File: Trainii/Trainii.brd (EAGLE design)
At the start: 50.8 x 71.1 mm, 44 parts, among them J1 APDS-9960, J2 Left Motor Encoder, J3 Right Motor Encoder, J4 Line Sensor 1, J5 Line Sensor 2, J6 Ultrasonic, J7 Left Motor Output, J8 Right Motor Output, J9 Lift Motor Output, U1 TPS61222DCKR, U2 BSS138, X1 JST-PH2

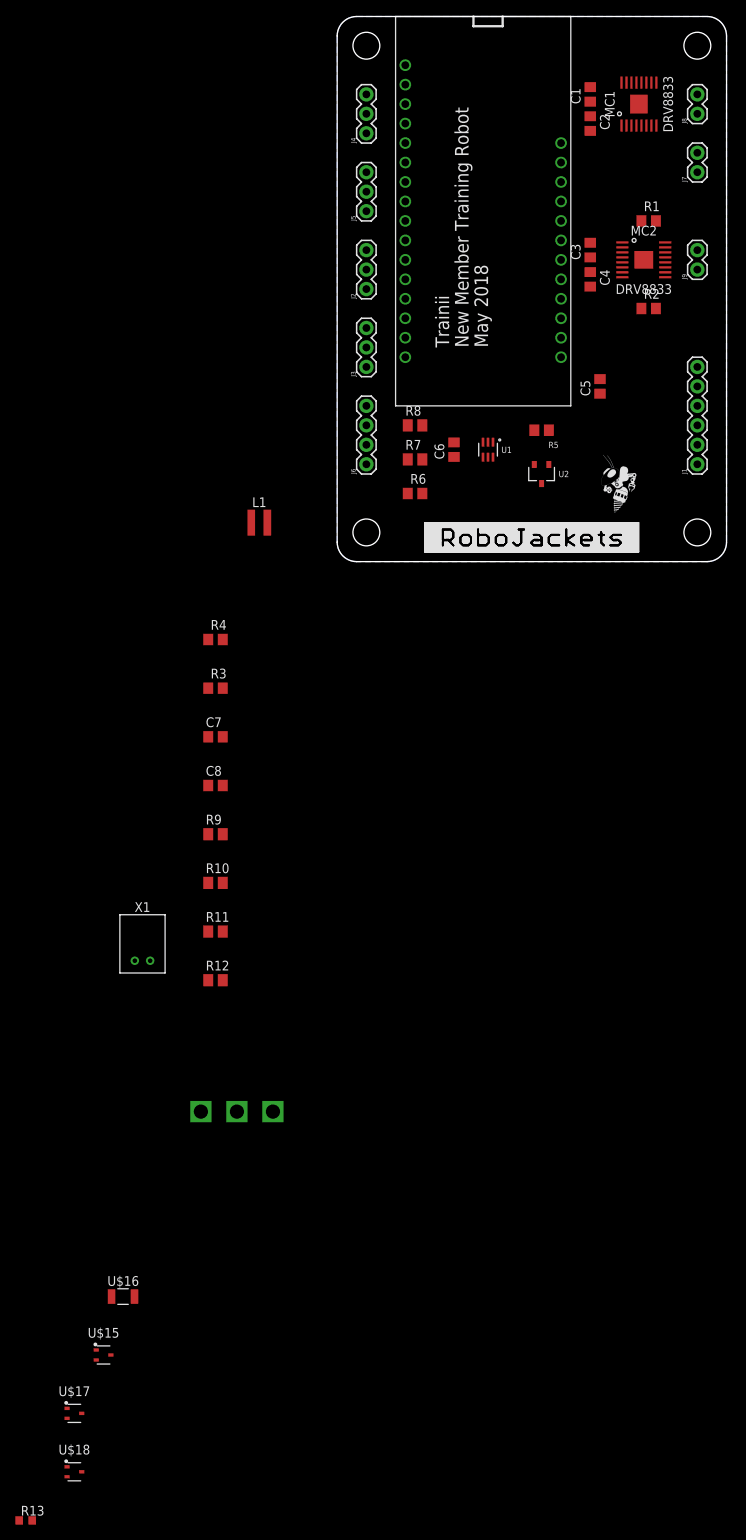
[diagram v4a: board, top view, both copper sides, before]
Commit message: Updated Libraries, corrected component placement
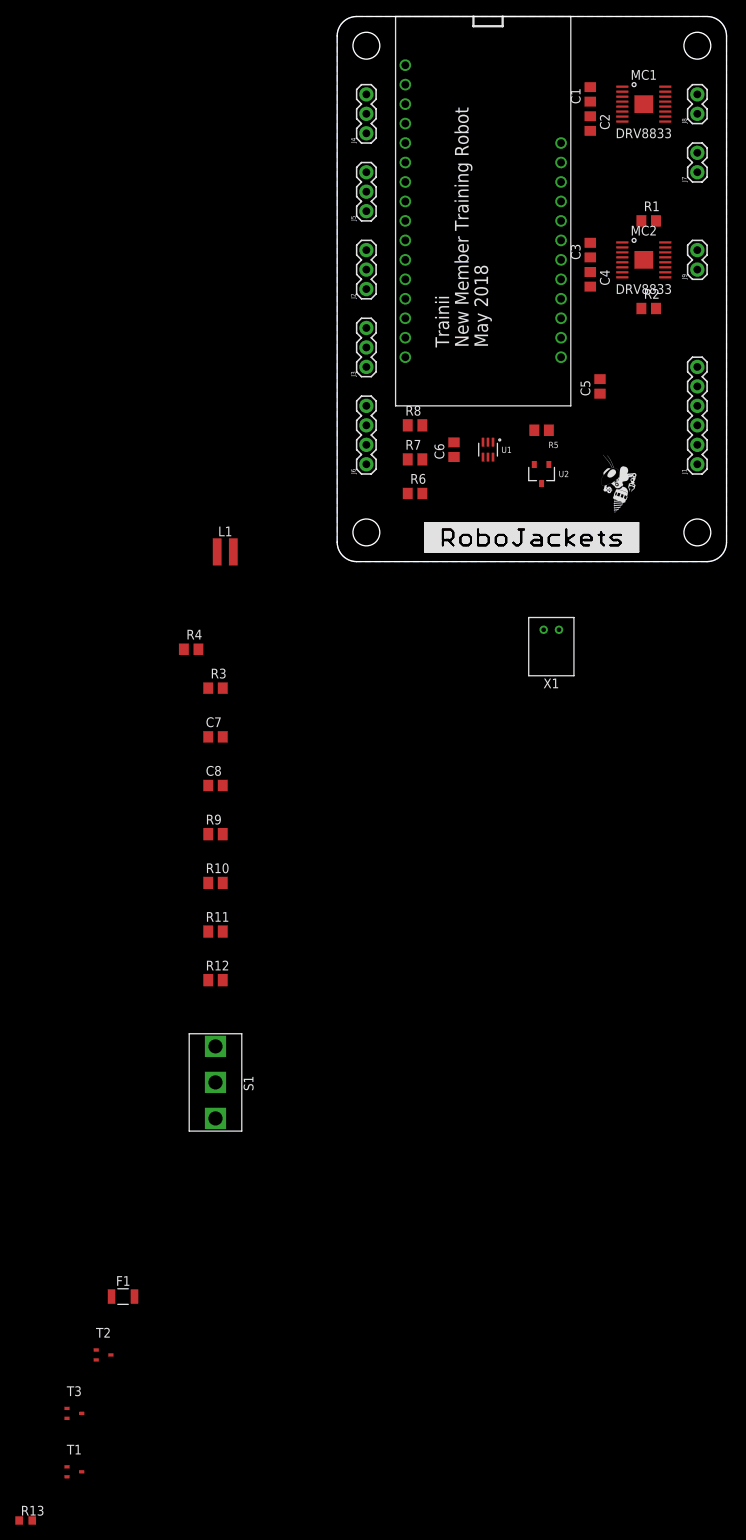
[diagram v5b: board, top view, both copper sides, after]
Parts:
- removed U$14: 100SP3T, Trainii:100SP3T
- added S1: 100SP3T, Trainii:100SP3T
- L1: value 4.7 uH -> 4.7uH
- R13: value (none) -> 10kΩ
- R3, R4: value 0.2 Ohm -> 0.2Ω
- moved X1 68.6 mm to (27.9, -8.89), turned to 180 degrees
- moved L1 5.85 mm to (-14.6, 1.27)
- moved R4 3.42 mm to (-19.1, -11.4)
- moved MC1 0.64 mm to (40.0, 59.7), turned to 0 degrees
- renumbered U$15 to T2, U$16 to F1, U$17 to T3, U$18 to T1
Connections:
- net VBAT_H renamed VBAT_HUZZAH
- new net VBAT_MOTOR_FUSE: C1.2, C2.1, C3.2, C4.1, F1.2, MC1.1, MC1.12, MC2.1, MC2.12
- net N$13: now also S1.3; no longer U$14.P$3
- net N$3: now also S1.1; no longer U$14.P$1
- net VBAT: now also S1.2; no longer F1.1, F1.2, U$14.P$2
- net VBAT_MOTOR: now also F1.1; no longer C1.2, C2.1, C3.2, C4.1, MC1.1, MC1.12, MC2.1, MC2.12

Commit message: Initial component placement before routing
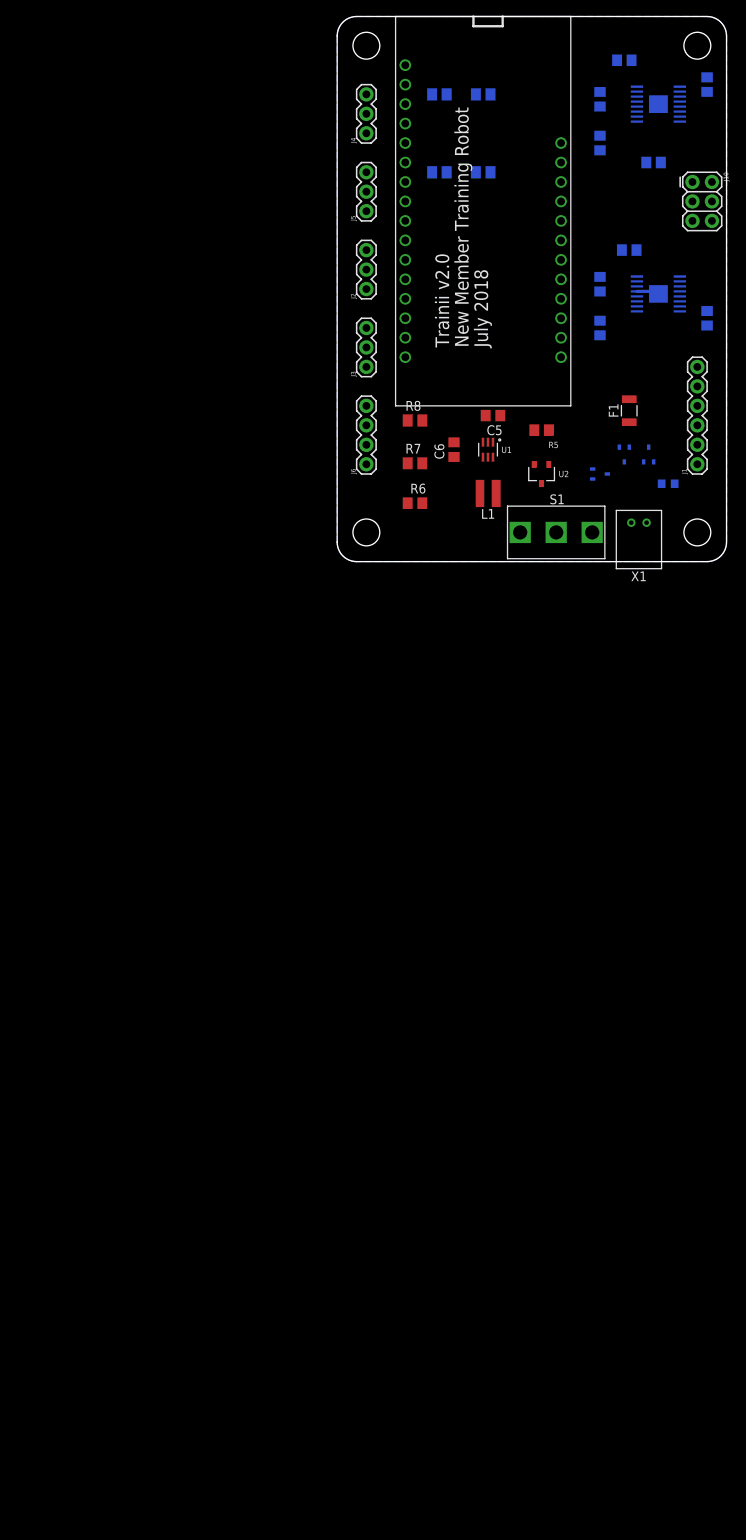
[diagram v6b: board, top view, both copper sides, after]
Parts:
- removed J7: Left Motor Output, SparkFun-Connectors:1X02
- removed J8: Right Motor Output, SparkFun-Connectors:1X02
- removed J9: Lift Motor Output, SparkFun-Connectors:1X02
- removed R13: 10kΩ, rcl:R0603
- removed U$2: (no value), RoboJackets-Aesthetics:ROBOBUZZ_0.4X
- removed U$8: (no value), RoboJackets-Aesthetics:ROBOJACKETS
- added J10: Motor Outputs, SparkFun-Connectors:2X3
- R1: value 0.2Ω -> 10kΩ; device rcl:R0805 -> rcl:R0603
- moved T1 152.4 mm to (40.6, 14.0), flipped to the bottom, turned to 90 degrees
- moved T3 144.2 mm to (37.5, 14.0), flipped to the bottom, turned to 270 degrees
- moved F1 133.1 mm to (38.1, 19.7), turned to 90 degrees
- moved T2 131.9 mm to (34.3, 11.4), flipped to the bottom, turned to 180 degrees
- moved R12 111.0 mm to (19.1, 50.8), flipped to the bottom, turned to 180 degrees
- moved R10 108.6 mm to (19.1, 61.0), flipped to the bottom, turned to 180 degrees
- moved R11 103.3 mm to (13.3, 50.8), flipped to the bottom, turned to 180 degrees
- moved C7 103.1 mm to (37.5, 65.4), flipped to the bottom, turned to 180 degrees
- moved R9 100.8 mm to (13.3, 61.0), flipped to the bottom
- moved R4 99.8 mm to (48.3, 62.2), flipped to the bottom, turned to 90 degrees
- moved R3 89.3 mm to (41.3, 52.1), flipped to the bottom
- moved C8 88.3 mm to (38.1, 40.6), flipped to the bottom, turned to 180 degrees
- moved S1 84.4 mm to (28.6, 3.81), turned to 0 degrees
- moved L1 35.1 mm to (19.7, 8.89), turned to 180 degrees
- moved R1 34.4 mm to (43.2, 10.2), flipped to the bottom
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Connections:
- removed net N$2: R1.1, R2.1
- removed net N$4: MC2.6, R1.2
- net GND: now also R1.1, R2.1; no longer R13.1
- net LEFT_0: now also J10.1; no longer J7.1
- net LEFT_1: now also J10.2; no longer J7.2
- net LIFT_0: now also J10.5; no longer J9.1
- net LIFT_1: now also J10.6; no longer J9.2
- net N$13: now also R1.2; no longer R13.2
- net RIGHT_0: now also J10.3; no longer J8.1
- net RIGHT_1: now also J10.4; no longer J8.2
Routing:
- net GND: track 0.00 -> 3.19 mm
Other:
- board text added: "July 2018"
- board text added: "Trainii v2.0"
- board text removed: "May 2018"
- board text removed: "Trainii"

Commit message: Initial routing
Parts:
- moved R4 5.68 mm to (43.2, 64.8), turned to 0 degrees
- moved R3 2.01 mm to (41.9, 54.0)
- turned R9 to 180 degrees
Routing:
- net 3V3: track 0.00 -> 115.4 mm
- net VBAT_MOTOR_FUSE: track 0.00 -> 83.6 mm, vias 0 -> 3
- net +5V: track 0.00 -> 73.1 mm
- net MOTOR_FAULT: track 0.00 -> 68.5 mm, vias 0 -> 4
- net TRIG_3V3: track 0.00 -> 51.8 mm, vias 0 -> 4
- net VBAT_HUZZAH: track 0.00 -> 46.7 mm
- net ECHO_3V3: track 0.00 -> 37.0 mm, vias 0 -> 2
- net LEFT_A: track 0.00 -> 34.3 mm, vias 0 -> 1
- net TRIG_5V: track 0.00 -> 29.6 mm, vias 0 -> 1
- net RIGHT_B: track 0.00 -> 26.7 mm, vias 0 -> 1
- net SDA: track 0.00 -> 23.3 mm
- net SCL: track 0.00 -> 22.5 mm
- net N$13: track 0.00 -> 21.2 mm, vias 0 -> 1
- net N$3: track 0.00 -> 21.0 mm, vias 0 -> 2
- net RIGHT_A: track 0.00 -> 20.0 mm, vias 0 -> 1
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
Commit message: Finished routing, exported images
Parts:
- removed J10: Motor Outputs, SparkFun-Connectors:2X3
- added J7: Left Motor, SparkFun-Connectors:1X02
- added J8: Right Motor, SparkFun-Connectors:1X02
- added J9: Lift Motor, SparkFun-Connectors:1X02
- C5: value 10uF 6.3V -> 10uF 16V
- J2: value Left Motor Encoder -> Left Mtr Encoder
- J3: value Right Motor Encoder -> Right Mtr Encoder
- R1: device rcl:R0603 -> rcl:R0805
- moved C4 5.12 mm to (39.4, 29.8), turned to 180 degrees
- moved C7 3.81 mm to (37.5, 61.6)
- moved C1 3.18 mm to (34.3, 57.1)
- moved R3 3.18 mm to (41.9, 50.8)
- moved F1 3.18 mm to (38.1, 22.9), flipped to the bottom
- moved C2 3.17 mm to (34.3, 51.4)
- moved MC1 3.17 mm to (41.9, 56.5)
- moved R4 3.17 mm to (43.2, 61.6)
- renumbered U$6 to M1
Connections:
- removed net LINE_OUT_1: M1.A2
- removed net LINE_OUT_2: M1.A3
- net LEFT_0: now also J7.1; no longer J10.1
- net LEFT_1: now also J7.2; no longer J10.2
- net LIFT_0: now also J9.1; no longer J10.5
- net LIFT_1: now also J9.2; no longer J10.6
- net LINE_OUT_1_3V3: now also M1.A2
- net LINE_OUT_2_3V3: now also M1.A3
- net RIGHT_0: now also J8.1; no longer J10.3
- net RIGHT_1: now also J8.2; no longer J10.4
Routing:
- net LINE_OUT_1_3V3: track 3.82 -> 19.0 mm, vias 0 -> 1
- net LEFT_1: track 13.0 -> 4.47 mm, vias 1 -> 0
- net LEFT_0: track 13.7 -> 5.40 mm
- net LINE_OUT_2_3V3: track 3.82 -> 11.1 mm
- net RIGHT_0: track 13.1 -> 5.82 mm
- net VBAT_MOTOR_FUSE: track 83.6 -> 77.0 mm, vias 3 -> 2
- net MOTOR_FAULT: track 68.5 -> 62.5 mm, vias 4 -> 2
- net 3V3: track 115.4 -> 109.7 mm
- net RIGHT_1: track 15.7 -> 10.2 mm, vias 2 -> 0
- net LIFT_1: track 12.1 -> 7.38 mm
- net VBAT_MOTOR: track 3.27 -> 6.44 mm, vias 1 -> 0
- net RIGHT_B: track 26.7 -> 23.5 mm
- net LEFT_B: track 19.0 -> 16.0 mm
- net LEFT_A: track 34.3 -> 33.0 mm
- net RIGHT_A: track 20.0 -> 18.7 mm
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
